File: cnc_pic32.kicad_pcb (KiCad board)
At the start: 4 copper layers, 96 x 96 mm, 128 parts, among them J1 icd, J10 tp_ft232_, J11 tp_ft232_, J12 tp_ft232_, J13 tp_ft232_, J14 tp_ft232_, J15 pololu, J16 pololu, J17 pololu, J18 pololu, J19 pololu, J2 USB_B_Mini, J20 pololu, J21 conector oled ST1306 128x32, J22 Adafruit ST7789, J23 conector oled ST1306 128x32, J24 Adafruit ST7789, J3 tp_ft232_, J4 tp_ft232_, J5 USB_B_Mini, J6 tp_ft232_, J7 tp_ft232_, J8 tp_ft232_, J9 tp_ft232_, Q1 2N7002, SW1 power, SW2 up, SW3 down, SW4 left, SW5 rigth, U1 PIC32MX795F512L-80x-PF, U2 LM1117DT-3.3, U3 FT232BM, U4 LM1117DT-3.3, U5 MRF24J40MA, Y1 8MHZ, Y2 6MHZ

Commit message: fix: unify +3.3V to +3V3 across all schematics and PCB
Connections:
- A1 pad 8: +3.3V -> +3V3
- A2 pad 8: +3.3V -> +3V3
- A3 pad 8: +3.3V -> +3V3
- A4 pad 8: +3.3V -> +3V3
- A5 pad 8: +3.3V -> +3V3
- C1 pad 1: +3.3V -> +3V3
- C10 pad 1: +3.3V -> +3V3
- C11 pad 1: +3.3V -> +3V3
- C2 pad 1: +3.3V -> +3V3
- C27 pad 1: +3.3V -> +3V3
- C28 pad 1: +3.3V -> +3V3
- C3 pad 1: +3.3V -> +3V3
- C4 pad 1: +3.3V -> +3V3
- C5 pad 1: +3.3V -> +3V3
- C6 pad 1: +3.3V -> +3V3
- C7 pad 1: +3.3V -> +3V3
- C8 pad 1: +3.3V -> +3V3
- C9 pad 1: +3.3V -> +3V3
- J1 pad 2: +3.3V -> +3V3
- J15 pad 2: +3.3V -> +3V3
- J21 pad 2: +3.3V -> +3V3
- J22 pad 2: +3.3V -> +3V3
- J23 pad 2: +3.3V -> +3V3
- J24 pad 2: +3.3V -> +3V3
- R1 pad 1: +3.3V -> +3V3
- R10 pad 1: +3.3V -> +3V3
- R11 pad 1: +3.3V -> +3V3
- R14 pad 1: +3.3V -> +3V3
- R15 pad 1: +3.3V -> +3V3
- R31 pad 1: +3.3V -> +3V3
- R32 pad 1: +3.3V -> +3V3
- R34 pad 2: +3.3V -> +3V3
- R35 pad 2: +3.3V -> +3V3
- R36 pad 1: +3.3V -> +3V3
- R37 pad 1: +3.3V -> +3V3
- R38 pad 1: +3.3V -> +3V3
- R39 pad 1: +3.3V -> +3V3
- R41 pad 1: +3.3V -> +3V3
- R42 pad 1: +3.3V -> +3V3
- R57 pad 1: +3.3V -> +3V3
- R58 pad 1: +3.3V -> +3V3
- R62 pad 1: +3.3V -> +3V3
- R63 pad 1: +3.3V -> +3V3
- U1 pad 16: +3.3V -> +3V3
- U1 pad 2: +3.3V -> +3V3
- U1 pad 30: +3.3V -> +3V3
- U1 pad 37: +3.3V -> +3V3
- U1 pad 46: +3.3V -> +3V3
- U1 pad 55: +3.3V -> +3V3
- U1 pad 62: +3.3V -> +3V3
- U1 pad 85: +3.3V -> +3V3
- U1 pad 86: +3.3V -> +3V3
- U5 pad 10: +3.3V -> +3V3
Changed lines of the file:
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@@
 			(layers "F.Cu" "F.Mask" "F.Paste")
 			(roundrect_rratio 0.243902)
-			(net "+3.3V")
+			(net "+3V3")
 			(pintype "passive")
 		)
@@
 			(layers "F.Cu" "F.Mask" "F.Paste")
 			(roundrect_rratio 0.25)
-			(net "+3.3V")
+			(net "+3V3")
 			(pintype "passive")
 		)
@@
 			(layers "F.Cu" "F.Mask" "F.Paste")
 			(roundrect_rratio 0.25)
-			(net "+3.3V")
+			(net "+3V3")
 			(pintype "passive")
 		)
@@
 			(layers "*.Cu" "*.Mask")
 			(remove_unused_layers no)
-			(net "+3.3V")
+			(net "+3V3")
 			(pinfunction "Pin_2_2")
 			(pintype "passive")
@@
 			(layers "F.Cu" "F.Mask" "F.Paste")
 			(roundrect_rratio 0.243902)
-			(net "+3.3V")
+			(net "+3V3")
 			(pintype "passive")
 		)
@@
 			(layers "F.Cu" "F.Mask" "F.Paste")
 			(roundrect_rratio 0.25)
-			(net "+3.3V")
+			(net "+3V3")
 			(pintype "passive")
 		)
@@
 			(layers "F.Cu" "F.Mask" "F.Paste")
 			(roundrect_rratio 0.243902)
-			(net "+3.3V")
+			(net "+3V3")
 			(pintype "passive")
 		)
@@
 			(layers "F.Cu" "F.Mask" "F.Paste")
 			(roundrect_rratio 0.243902)
-			(net "+3.3V")
+			(net "+3V3")
 			(pintype "passive")
 		)
@@
 			(layers "*.Cu" "*.Mask")
 			(remove_unused_layers no)
-			(net "+3.3V")
+			(net "+3V3")
 			(pinfunction "VMOT_8")
 			(pintype "power_in")
@@
 			(layers "F.Cu" "F.Mask" "F.Paste")
 			(roundrect_rratio 0.25)
-			(net "+3.3V")
+			(net "+3V3")
 			(pintype "passive")
 		)
@@
 			(layers "F.Cu" "F.Mask" "F.Paste")
 			(roundrect_rratio 0.25)
-			(net "+3.3V")
+			(net "+3V3")
 			(pintype "passive")
 		)
@@
 			(layers "F.Cu" "F.Mask" "F.Paste")
 			(roundrect_rratio 0.243902)
-			(net "+3.3V")
+			(net "+3V3")
 			(pintype "passive")
 		)
@@
 			(layers "F.Cu" "F.Mask" "F.Paste")
 			(roundrect_rratio 0.25)
-			(net "+3.3V")
+			(net "+3V3")
 			(pintype "passive")
 		)
@@
 			(layers "F.Cu" "F.Mask" "F.Paste")
 			(roundrect_rratio 0.25)
-			(net "+3.3V")
+			(net "+3V3")
 			(pintype "passive")
 		)
@@
 			(layers "F.Cu" "F.Mask" "F.Paste")
 			(roundrect_rratio 0.243902)
-			(net "+3.3V")
+			(net "+3V3")
 			(pintype "passive")
 		)
@@
 			(layers "F.Cu" "F.Mask" "F.Paste")
 			(roundrect_rratio 0.25)
-			(net "+3.3V")
+			(net "+3V3")
 			(pintype "passive")
 		)
@@
 			(layers "F.Cu" "F.Mask" "F.Paste")
 			(roundrect_rratio 0.243902)
-			(net "+3.3V")
+			(net "+3V3")
 			(pintype "passive")
 		)
@@
 			(layers "*.Cu" "*.Mask")
 			(remove_unused_layers no)
-			(net "+3.3V")
+			(net "+3V3")
 			(pinfunction "Pin_2_2")
 			(pintype "passive")
@@
 			(layers "F.Cu" "F.Mask" "F.Paste")
 			(roundrect_rratio 0.243902)
-			(net "+3.3V")
+			(net "+3V3")
 			(pintype "passive")
 		)
@@
 			(layers "F.Cu" "F.Mask" "F.Paste")
 			(roundrect_rratio 0.25)
-			(net "+3.3V")
+			(net "+3V3")
 			(pintype "passive")
 		)
@@
 			(layers "F.Cu" "F.Mask" "F.Paste")
 			(roundrect_rratio 0.25)
-			(net "+3.3V")
+			(net "+3V3")
 			(pintype "passive")
 		)
@@
 			(layers "F.Cu" "F.Mask" "F.Paste")
 			(roundrect_rratio 0.243902)
-			(net "+3.3V")
+			(net "+3V3")
 			(pintype "passive")
 		)
@@
 			(layers "*.Cu" "*.Mask")
 			(remove_unused_layers no)
-			(net "+3.3V")
+			(net "+3V3")
 			(pinfunction "VMOT_8")
 			(pintype "power_in")
@@
 			(layers "F.Cu" "F.Mask" "F.Paste")
 			(roundrect_rratio 0.25)
-			(net "+3.3V")
+			(net "+3V3")
 			(pintype "passive")
 		)
@@
 			(size 2.032 2.032)
 			(layers "F.Cu" "F.Mask" "F.Paste")
-			(net "+3.3V")
+			(net "+3V3")
 			(pinfunction "VIN_10")
 			(pintype "power_in")
@@
 			(layers "F.Cu" "F.Mask" "F.Paste")
 			(roundrect_rratio 0.243902)
-			(net "+3.3V")
+			(net "+3V3")
 			(pintype "passive")
 		)
@@
 			(layers "F.Cu" "F.Mask" "F.Paste")
 			(roundrect_rratio 0.25)
-			(net "+3.3V")
+			(net "+3V3")
 			(pintype "passive")
 		)
@@
 			(layers "*.Cu" "*.Mask")
 			(remove_unused_layers no)
-			(net "+3.3V")
+			(net "+3V3")
 			(pinfunction "Pin_2_2")
 			(pintype "passive")
@@
 			(layers "F.Cu" "F.Mask" "F.Paste")
 			(roundrect_rratio 0.25)
-			(net "+3.3V")
+			(net "+3V3")
 			(pintype "passive")
 		)
@@
 			(layers "F.Cu" "F.Mask" "F.Paste")
 			(roundrect_rratio 0.243902)
-			(net "+3.3V")
+			(net "+3V3")
 			(pintype "passive")
 		)
@@
 			(layers "F.Cu" "F.Mask" "F.Paste")
 			(roundrect_rratio 0.25)
-			(net "+3.3V")
+			(net "+3V3")
 			(pintype "passive")
 		)
@@
 			(layers "F.Cu" "F.Mask" "F.Paste")
 			(roundrect_rratio 0.243902)
-			(net "+3.3V")
+			(net "+3V3")
 			(pintype "passive")
 		)
@@
 			(layers "F.Cu" "F.Mask" "F.Paste")
 			(roundrect_rratio 0.243902)
-			(net "+3.3V")
+			(net "+3V3")
 			(pintype "passive")
 		)
@@
 			(layers "*.Cu" "*.Mask")
 			(remove_unused_layers no)
-			(net "+3.3V")
+			(net "+3V3")
 			(pinfunction "Pin_2_2")
 			(pintype "passive")
@@
 			(layers "*.Cu" "*.Mask")
 			(remove_unused_layers no)
-			(net "+3.3V")
+			(net "+3V3")
 			(pinfunction "VMOT_8")
 			(pintype "power_in")
@@
 			(layers "F.Cu" "F.Mask" "F.Paste")
 			(roundrect_rratio 0.243902)
-			(net "+3.3V")
+			(net "+3V3")
 			(pintype "passive")
 		)
@@
 			(layers "F.Cu" "F.Mask" "F.Paste")
 			(roundrect_rratio 0.25)
-			(net "+3.3V")
+			(net "+3V3")
 			(pinfunction "VDD_2")
 			(pintype "power_in")
@@
 			(layers "F.Cu" "F.Mask" "F.Paste")
 			(roundrect_rratio 0.25)
-			(net "+3.3V")
+			(net "+3V3")
 			(pinfunction "VDD_16")
 			(pintype "power_in")
@@
 			(layers "F.Cu" "F.Mask" "F.Paste")
 			(roundrect_rratio 0.25)
-			(net "+3.3V")
+			(net "+3V3")
 			(pinfunction "AVDD_30")
 			(pintype "power_in")
@@
 			(layers "F.Cu" "F.Mask" "F.Paste")
 			(roundrect_rratio 0.25)
-			(net "+3.3V")
+			(net "+3V3")
 			(pinfunction "VDD_37")
 			(pintype "power_in")
@@
 			(layers "F.Cu" "F.Mask" "F.Paste")
 			(roundrect_rratio 0.25)
-			(net "+3.3V")
+			(net "+3V3")
 			(pinfunction "VDD_46")
 			(pintype "power_in")
@@
 			(layers "F.Cu" "F.Mask" "F.Paste")
 			(roundrect_rratio 0.25)
-			(net "+3.3V")
+			(net "+3V3")
 			(pinfunction "VUSB3V3_55")
 			(pintype "power_in")
@@
 			(layers "F.Cu" "F.Mask" "F.Paste")
 			(roundrect_rratio 0.25)
-			(net "+3.3V")
+			(net "+3V3")
 			(pinfunction "VDD_62")
 			(pintype "power_in")
@@
 			(layers "F.Cu" "F.Mask" "F.Paste")
 			(roundrect_rratio 0.25)
-			(net "+3.3V")
+			(net "+3V3")
 			(pinfunction "VCAP/VDDCORE_85")
 			(pintype "power_out")
@@
 			(layers "F.Cu" "F.Mask" "F.Paste")
 			(roundrect_rratio 0.25)
-			(net "+3.3V")
+			(net "+3V3")
 			(pinfunction "VDD_86")
 			(pintype "power_in")
@@
 			(layers "F.Cu" "F.Mask" "F.Paste")
 			(roundrect_rratio 0.25)
-			(net "+3.3V")
+			(net "+3V3")
 			(pintype "passive")
 		)
@@
 			(layers "*.Cu" "*.Mask")
 			(remove_unused_layers no)
-			(net "+3.3V")
+			(net "+3V3")
 			(pinfunction "Pin_2_2")
 			(pintype "passive")
@@
 			(layers "*.Cu" "*.Mask")
 			(remove_unused_layers no)
-			(net "+3.3V")
+			(net "+3V3")
 			(pinfunction "VMOT_8")
 			(pintype "power_in")
@@
 			(layers "F.Cu" "F.Mask" "F.Paste")
 			(roundrect_rratio 0.25)
-			(net "+3.3V")
+			(net "+3V3")
 			(pintype "passive")
 		)
@@
 			(layers "F.Cu" "F.Mask" "F.Paste")
 			(roundrect_rratio 0.25)
-			(net "+3.3V")
+			(net "+3V3")
 			(pintype "passive")
 		)
@@
 			(layers "F.Cu" "F.Mask" "F.Paste")
 			(roundrect_rratio 0.243902)
-			(net "+3.3V")
+			(net "+3V3")
 			(pintype "passive")
 		)
@@
 			(layers "*.Cu" "*.Mask")
 			(remove_unused_layers no)
-			(net "+3.3V")
+			(net "+3V3")
 			(pinfunction "VMOT_8")
 			(pintype "power_in")
@@
 			(layers "*.Cu" "*.Mask")
 			(remove_unused_layers no)
-			(net "+3.3V")
+			(net "+3V3")
 			(pinfunction "Pin_2_2")
 			(pintype "passive")

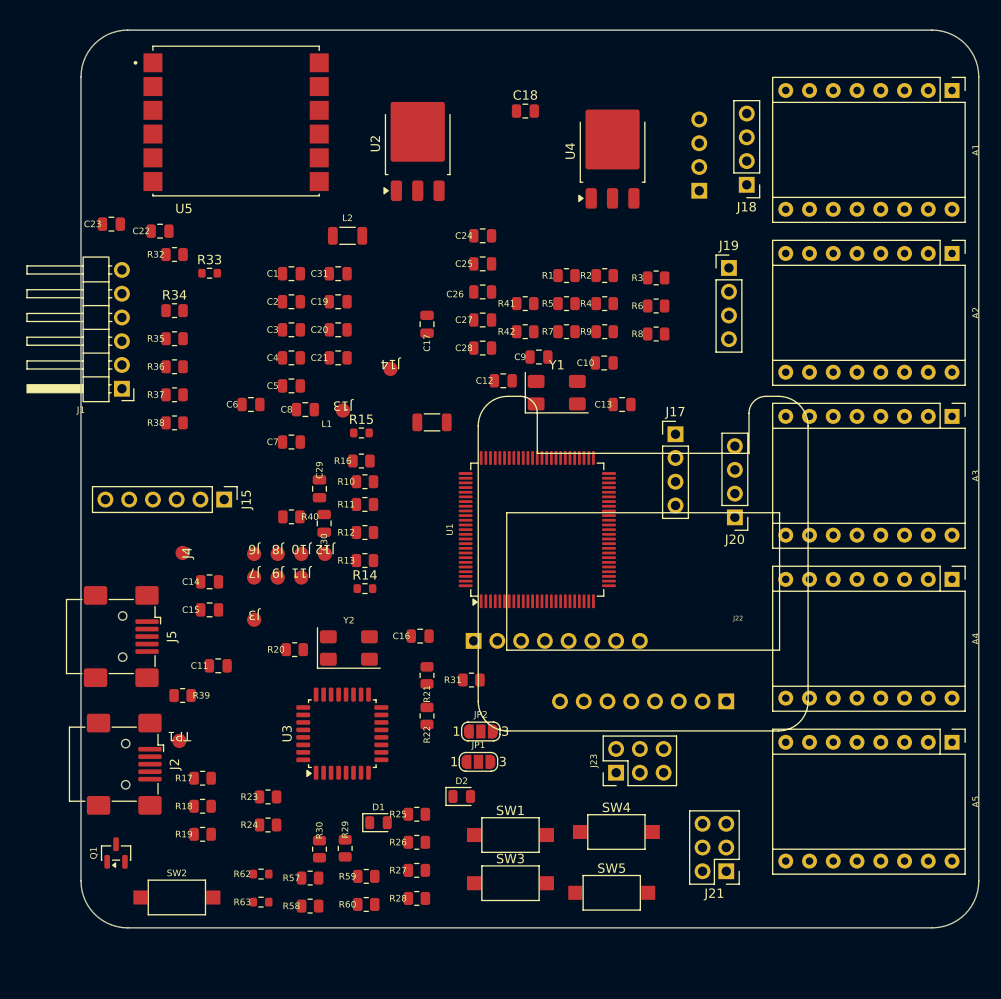
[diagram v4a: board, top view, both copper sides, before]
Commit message: feat: integrate zigbee sheet + R 0603→0805 footprint update
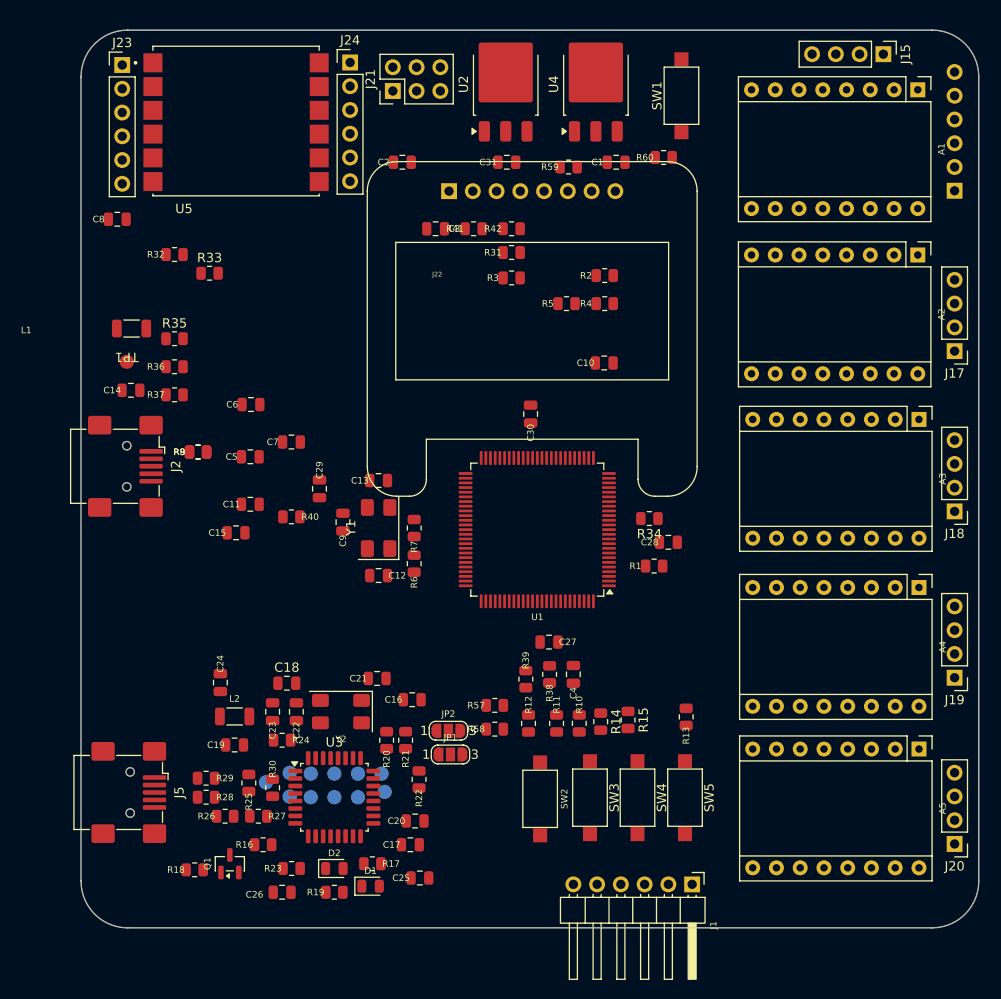
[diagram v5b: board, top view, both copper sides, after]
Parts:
- removed R62, R63: 2k2, Resistor_SMD:R_0603_1608Metric
- J10, J11, J12, J13, J14, J3, J4, J6, J7, J8, J9: moved to B.Cu
- J15: footprint Library:PinHeader_1x06_P2.54mm_Vertical -> Connector_PinHeader_2.54mm:PinHeader_1x04_P2.54mm_Vertical
- J16: footprint Connector_PinHeader_2.54mm:PinHeader_1x04_P2.54mm_Vertical -> Library:PinHeader_1x06_P2.54mm_Vertical
- J23: value conector oled ST1306 128x32 -> mrf24j40_tp; footprint Connector_PinHeader_2.54mm:PinHeader_2x03_P2.54mm_Vertical -> Connector_PinHeader_2.54mm:PinHeader_1x06_P2.54mm_Vertical
- J24: value Adafruit ST7789 -> mrf24j40_tp; footprint Library:Adafruit_SSD1306_No_Mounting_Holes_pads -> Connector_PinHeader_2.54mm:PinHeader_1x06_P2.54mm_Vertical; moved to F.Cu
- R14, R15, R33: footprint Resistor_SMD:R_0603_1608Metric -> Resistor_SMD:R_0805_2012Metric
- R38, R39: value 1k -> 2k2
- moved J23 92.3 mm to (56.4, 29.7), turned to 0 degrees
- moved J21 90.7 mm to (85.3, 32.5), turned to 90 degrees
- moved R60 86.0 mm to (114.3, 39.6)
- moved J15 85.1 mm to (137.8, 28.6)
- moved SW1 81.1 mm to (116.2, 33.0), turned to 90 degrees
- moved J1 80.8 mm to (117.3, 117.3), turned to -90 degrees
- moved R59 78.9 mm to (104.1, 40.6)
- moved C26 67.7 mm to (73.5, 118.2)
- moved C18 66.3 mm to (74.0, 95.8)
- moved C25 66.0 mm to (88.2, 116.7)
- moved J24 63.2 mm to (80.8, 29.5)
- moved J22 62.1 mm to (91.4, 43.2), turned to 0 degrees
- moved C17 55.7 mm to (87.2, 113.1), turned to 0 degrees
- moved R34 55.4 mm to (112.8, 78.2), turned to 180 degrees
- moved C24 55.4 mm to (66.9, 95.8), turned to -90 degrees
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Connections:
- A1 pad 8: +3V3 -> +3.3V
- A2 pad 8: +3V3 -> +3.3V
- A3 pad 8: +3V3 -> +3.3V
- A4 pad 8: +3V3 -> +3.3V
- A5 pad 8: +3V3 -> +3.3V
- C1 pad 1: +3V3 -> +3.3V
- C10 pad 1: +3V3 -> +3.3V
- C11 pad 1: +3V3 -> +3.3V
- C13 pad 1: /MCU/OSC2 -> /MCU/OSC1
- C2 pad 1: +3V3 -> +3.3V
- C27 pad 1: +3V3 -> +3.3V
- C28 pad 1: +3V3 -> +3.3V
- C3 pad 1: +3V3 -> +3.3V
- C4 pad 1: +3V3 -> +3.3V
- C5 pad 1: +3V3 -> +3.3V
- C6 pad 1: +3V3 -> +3.3V
- C7 pad 1: +3V3 -> +3.3V
- C8 pad 1: +3V3 -> +3.3V
- C9 pad 1: +3V3 -> +3.3V
- J1 pad 2: +3V3 -> +3.3V
- J1 pad 4: /MCU/RB7 -> /MCU/RC2
- J1 pad 5: /MCU/RB6 -> /MCU/RC3
- J1 pad 6: /idc/RB4 -> /MCU/RC1
- J15 pad 1: +5V -> Net-(A1-2B)
- J15 pad 2: +3V3 -> Net-(A1-2A)
- J15 pad 3: unconnected-(J15-Pin_3-Pad3) -> Net-(A1-1A)
- J15 pad 4: unconnected-(J15-Pin_4-Pad4) -> Net-(A1-1B)
- J16 pad 1: Net-(A1-2B) -> +5V
- J16 pad 2: Net-(A1-2A) -> +3.3V
- J16 pad 3: Net-(A1-1A) -> unconnected-(J16-Pin_3-Pad3)
- J16 pad 4: Net-(A1-1B) -> unconnected-(J16-Pin_4-Pad4)
- J21 pad 2: +3V3 -> +3.3V
- J21 pad 5: unconnected-(J21-Pin_5-Pad5) -> /Oled/RG7
- J21 pad 6: unconnected-(J21-Pin_6-Pad6) -> /Oled/RG8
- J22 pad 2: +3V3 -> +3.3V
- J22 pad 5: unconnected-(J22-Pin_5-Pad5) -> /Oled/RG0
- J22 pad 6: unconnected-(J22-Pin_6-Pad6) -> /Oled/RG1
- J22 pad 7: unconnected-(J22-Pin_7-Pad7) -> /Oled/RG6
- J23 pad 2: +3V3 -> /MCU/RF4
- J23 pad 3: /MCU/scl -> /MCU/RF5
- J23 pad 4: /MCU/sda -> /MCU/RF12
- J23 pad 5: unconnected-(J23-Pin_5-Pad5) -> /MCU/RF0
- J23 pad 6: unconnected-(J23-Pin_6-Pad6) -> /MCU/RF1
- J24 pad 2: +3V3 -> GND
- J24 pad 3: /MCU/sda -> +3.3V
- J24 pad 4: /MCU/scl -> unconnected-(J24-Pin_4-Pad4)
- J24 pad 5: unconnected-(J24-Pin_5-Pad5) -> /MCU/RF3
- J24 pad 6: unconnected-(J24-Pin_6-Pad6) -> /MCU/RF2
- R1 pad 1: +3V3 -> +3.3V
- R10 pad 1: +3V3 -> +3.3V
- R11 pad 1: +3V3 -> +3.3V
- R14 pad 1: +3V3 -> +3.3V
- R15 pad 1: +3V3 -> +3.3V
- R31 pad 1: +3V3 -> +3.3V
- R32 pad 1: +3V3 -> +3.3V
- R33 pad 1: /MCU/RA6 -> +3.3V
- R33 pad 2: GND -> /MCU/RF4
- R34 pad 1: /MCU/RA2 -> +3.3V
- R34 pad 2: +3V3 -> /MCU/RF12
- R35 pad 1: /MCU/RA0 -> /MCU/RF5
- R35 pad 2: +3V3 -> GND
- R36 pad 1: +3V3 -> /MCU/RF2
- R36 pad 2: /MCU/RA5 -> +3.3V
- R37 pad 1: +3V3 -> /MCU/RF3
- R37 pad 2: /MCU/RA3 -> +3.3V
- R38 pad 1: +3V3 -> +3.3V
- R38 pad 2: /MCU/scl -> /MCU/RF1
- R39 pad 1: +3V3 -> +3.3V
- R39 pad 2: /MCU/sda -> /MCU/RF0
- R6 pad 1: /MCU/OSC1 -> /MCU/OSC2
- R7 pad 2: /MCU/OSC2 -> /MCU/OSC1
- U1 pad 16: +3V3 -> +3.3V
- U1 pad 2: +3V3 -> +3.3V
- U1 pad 26: /MCU/RB6 -> /Ft232/TX_MCU
- U1 pad 27: /MCU/RB7 -> /Ft232/RX_MCU
- U1 pad 30: +3V3 -> +3.3V
- U1 pad 37: +3V3 -> +3.3V
- U1 pad 46: +3V3 -> +3.3V
- U1 pad 55: +3V3 -> +3.3V
- U1 pad 62: +3V3 -> +3.3V
- U1 pad 85: +3V3 -> +3.3V
- U1 pad 86: +3V3 -> +3.3V
- U1 pad 87: /Ft232/RX_MCU -> /MCU/RF0
- U1 pad 88: /Ft232/TX_MCU -> /MCU/RF1
- U5 pad 10: +3V3 -> +3.3V
- U5 pad 2: /MCU/RA4 -> /MCU/RF4
- U5 pad 3: /MCU/RA6 -> /MCU/RF5
- U5 pad 4: /MCU/RA1 -> /MCU/RF12
- U5 pad 5: /MCU/RA3 -> /MCU/RF0
- U5 pad 6: /MCU/RA5 -> /MCU/RF1
- U5 pad 7: /MCU/RA2 -> /MCU/RF2
- U5 pad 8: /MCU/RA0 -> /MCU/RF3
- Y1 pad 3: /MCU/OSC2 -> /MCU/OSC1

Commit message: feat: add orphaned PCB components to schematics - R4/R5 MCU, R41/R42 OLED, C37/C38 power
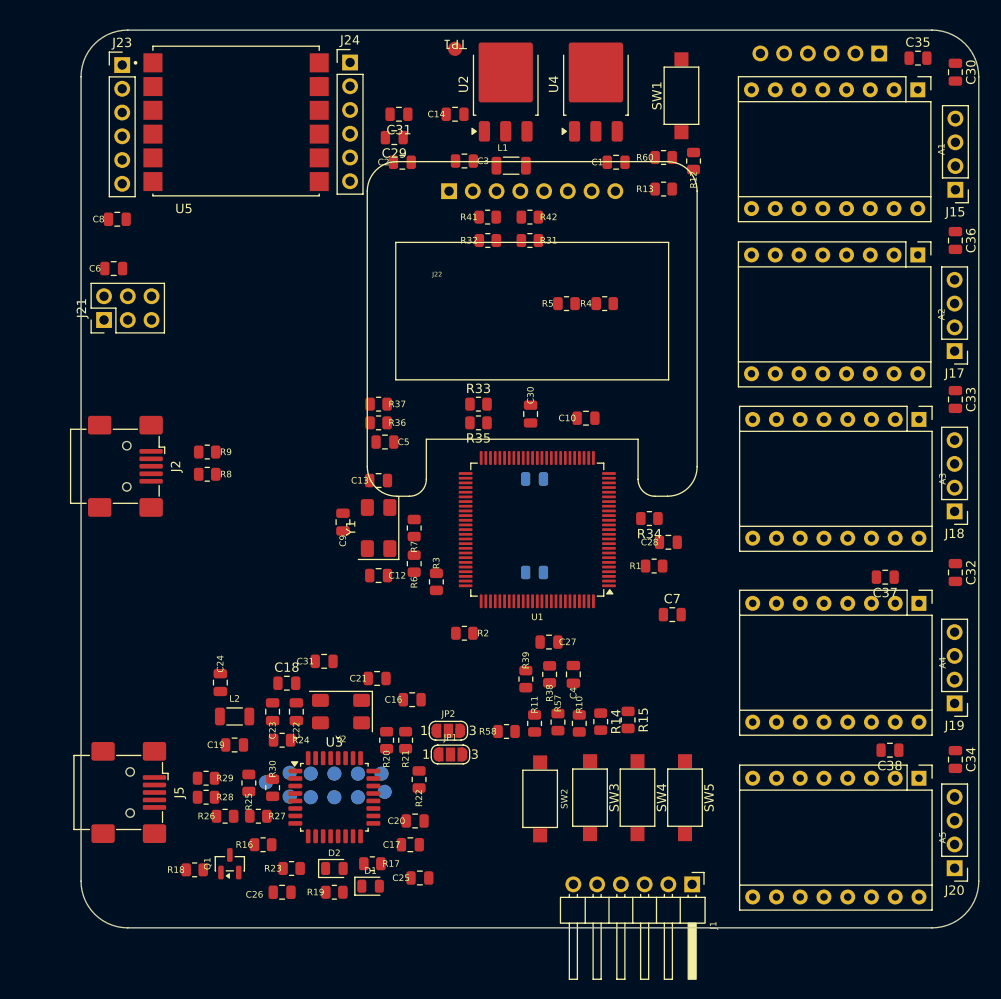
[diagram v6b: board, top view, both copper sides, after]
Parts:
- removed R40: 22, Resistor_SMD:R_0805_2012Metric
- removed R59: 2k2, Resistor_SMD:R_0805_2012Metric
- added C30: 100nf, Capacitor_SMD:C_0805_2012Metric, F.Cu at (145.5, 30.5)
- added C31: 100nf, Capacitor_SMD:C_0805_2012Metric, F.Cu at (86.0, 35.0)
- added C32: 100nf, Capacitor_SMD:C_0805_2012Metric, F.Cu at (145.5, 84.0)
- added C33: 100nf, Capacitor_SMD:C_0805_2012Metric, F.Cu at (145.5, 65.5)
- added C34: 100nf, Capacitor_SMD:C_0805_2012Metric, F.Cu at (145.5, 104.0)
- added C35: 100nf, Capacitor_SMD:C_0805_2012Metric, F.Cu at (141.5, 29.0)
- added C36: 100nf, Capacitor_SMD:C_0805_2012Metric, F.Cu at (145.5, 48.5)
- added C37: 100nf, Capacitor_SMD:C_0805_2012Metric, F.Cu at (138.0, 84.5)
- added C38: 100nf, Capacitor_SMD:C_0805_2012Metric, F.Cu at (138.5, 103.0)
- C11, C15: moved to B.Cu
- moved R12 62.7 mm to (117.5, 40.0), turned to 90 degrees
- moved C31 56.8 mm to (78.0, 93.5)
- moved R13 56.5 mm to (114.3, 43.0), turned to 0 degrees
- moved TP1 48.5 mm to (92.0, 28.0)
- moved C14 45.5 mm to (92.0, 35.0)
- moved C7 44.7 mm to (115.2, 88.5)
- moved L1 44.2 mm to (98.0, 40.5)
- moved R2 41.1 mm to (93.0, 90.5), turned to 180 degrees
- moved J21 39.4 mm to (54.5, 57.0)
- moved C29 38.4 mm to (85.5, 37.5), turned to 180 degrees
- moved R35 33.7 mm to (94.5, 68.0), turned to 180 degrees
- moved R32 33.5 mm to (95.5, 48.5)
- moved R3 33.5 mm to (90.0, 85.0), turned to -90 degrees
- moved C15 32.2 mm to (100.5, 84.0), turned to 180 degrees
- moved R33 32.0 mm to (94.5, 66.0)
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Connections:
- C29 pad 1: GND -> +5V
- C29 pad 2: Net-(TP17-Pin_1) -> GND
- J21 pad 3: /MCU/scl -> /MCU/sda
- J21 pad 4: /MCU/sda -> /Oled/RG7
- J21 pad 5: /Oled/RG7 -> /MCU/scl
